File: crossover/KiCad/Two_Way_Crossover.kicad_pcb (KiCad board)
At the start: 2 copper layers, 115.6 x 152.4 mm, 21 parts, among them J1 Conn_01x01_Female, J2 Conn_01x01_Female, J3 Woofer, J4 Tweeter

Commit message: Tweak crossover
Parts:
- moved J2 8.98 mm to (38.7, 105.4)
- moved J3 8.89 mm to (142.9, 78.7)
- moved C1 7.73 mm to (73.0, 95.2)
- moved J1 7.73 mm to (38.7, 95.2)
- moved L1 7.66 mm to (41.3, 67.3)
- moved C4 7.65 mm to (72.4, 38.1)
- moved J4 5.08 mm to (142.9, 95.2)
- moved H1 1.27 mm to (143.5, 29.2)
- moved H2 1.27 mm to (143.5, 171.4)
- moved C3 0.63 mm to (44.5, 117.5)
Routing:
- net Net-(J4-Pad1): track 57.2 -> 108.0 mm
- net Net-(J3-Pad1): track 72.5 -> 79.8 mm
- net Net-(C1-Pad1): track 48.6 -> 55.5 mm
- net Net-(C4-Pad1): track 11.2 -> 5.50 mm
- net Net-(C2-Pad2): track 91.1 -> 86.7 mm
- net Net-(C3-Pad2): track 19.4 -> 20.3 mm
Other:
- board size 115.6 x 152.4 mm -> 116.8 x 152.4 mm
- net class Default: clearance 0.2 -> 0.1524; trace_width 0.25 -> 0.1524; via_dia 0.8 -> 0.508; via_drill 0.4 -> 0.254
- rule pad_to_mask_clearance: 0.051 -> 0.0508
- rule trace_clearance: 0.2 -> 0.1524
- rule trace_min: 0.2 -> 0.1524
- rule via_min_drill: 0.3 -> 0.254
- rule via_min_size: 0.4 -> 0.508

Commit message: Redesign PCB
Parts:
- removed R5, R6: 8R2, Resistor_THT:R_Axial_Power_L60.0mm_W14.0mm_P66.04mm
- L1, L2, L3: footprint Inductor_THT:L_Radial_D40.6mm_P26.16mm_Vishay_IHB-5 -> etal_Inductors:Radial_D36.5mm_H12.0mm_P23.0mm
- R1, R2: footprint Resistor_THT:R_Axial_Power_L60.0mm_W14.0mm_P66.04mm -> etal_Power_Resistor:Resistor_Power_Axial_L91.5_W20.2_H20.2
- R3, R4: value 8R2 -> 4R7
- moved H1 110.5 mm to (33.0, 31.0)
- moved H3 93.2 mm to (130.0, 31.0)
- moved R3 73.4 mm to (113.5, 181.6)
- moved J4 70.1 mm to (126.0, 163.3)
- moved C2 66.5 mm to (114.8, 147.3), turned to 90 degrees
- moved C1 60.3 mm to (47.0, 149.6), turned to 90 degrees
- moved C3 56.6 mm to (100.8, 122.4), turned to 270 degrees
- moved R4 51.6 mm to (113.5, 165.9), turned to 180 degrees
- moved J3 49.9 mm to (126.0, 125.7)
- moved C4 48.9 mm to (49.5, 81.3), turned to 270 degrees
- moved L1 45.1 mm to (76.7, 95.2), turned to 180 degrees
- moved L3 33.0 mm to (114.6, 95.2), turned to 180 degrees
- moved J2 31.1 mm to (34.0, 136.1)
- moved J1 27.3 mm to (34.0, 122.2)
- moved R2 24.8 mm to (81.5, 65.0), turned to 180 degrees
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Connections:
- R4 pad 1: Net-(C3-Pad2) -> Net-(J4-Pad1)
- R4 pad 2: Net-(J4-Pad1) -> GND
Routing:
- net Net-(J4-Pad1): track 108.0 -> 28.2 mm
- net Net-(C3-Pad2): track 20.3 -> 66.5 mm
- net Net-(C2-Pad2): track 86.7 -> 126.9 mm
- net Net-(C4-Pad1): track 5.50 -> 24.8 mm
- net Net-(C1-Pad2): track 35.8 -> 50.0 mm
- net Net-(C1-Pad1): track 55.5 -> 66.4 mm
- net Net-(J3-Pad1): track 79.8 -> 89.7 mm
- removed copper zone on F.Cu, net GND
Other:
- board size 116.8 x 152.4 mm -> 107 x 167 mm

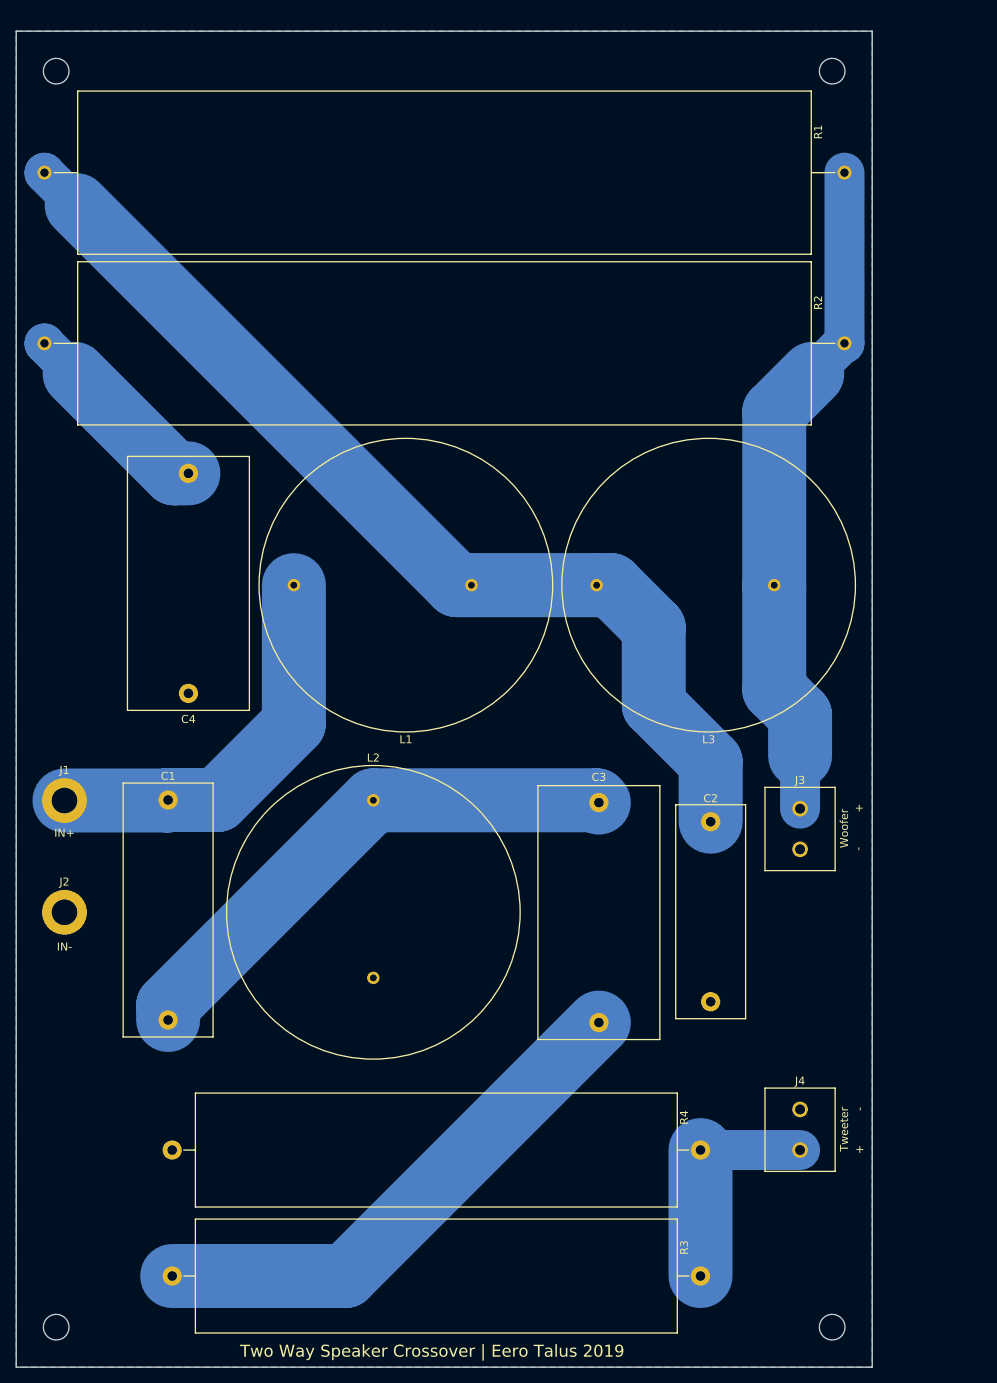
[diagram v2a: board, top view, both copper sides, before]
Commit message: Partially fix incorrect PCB footprints
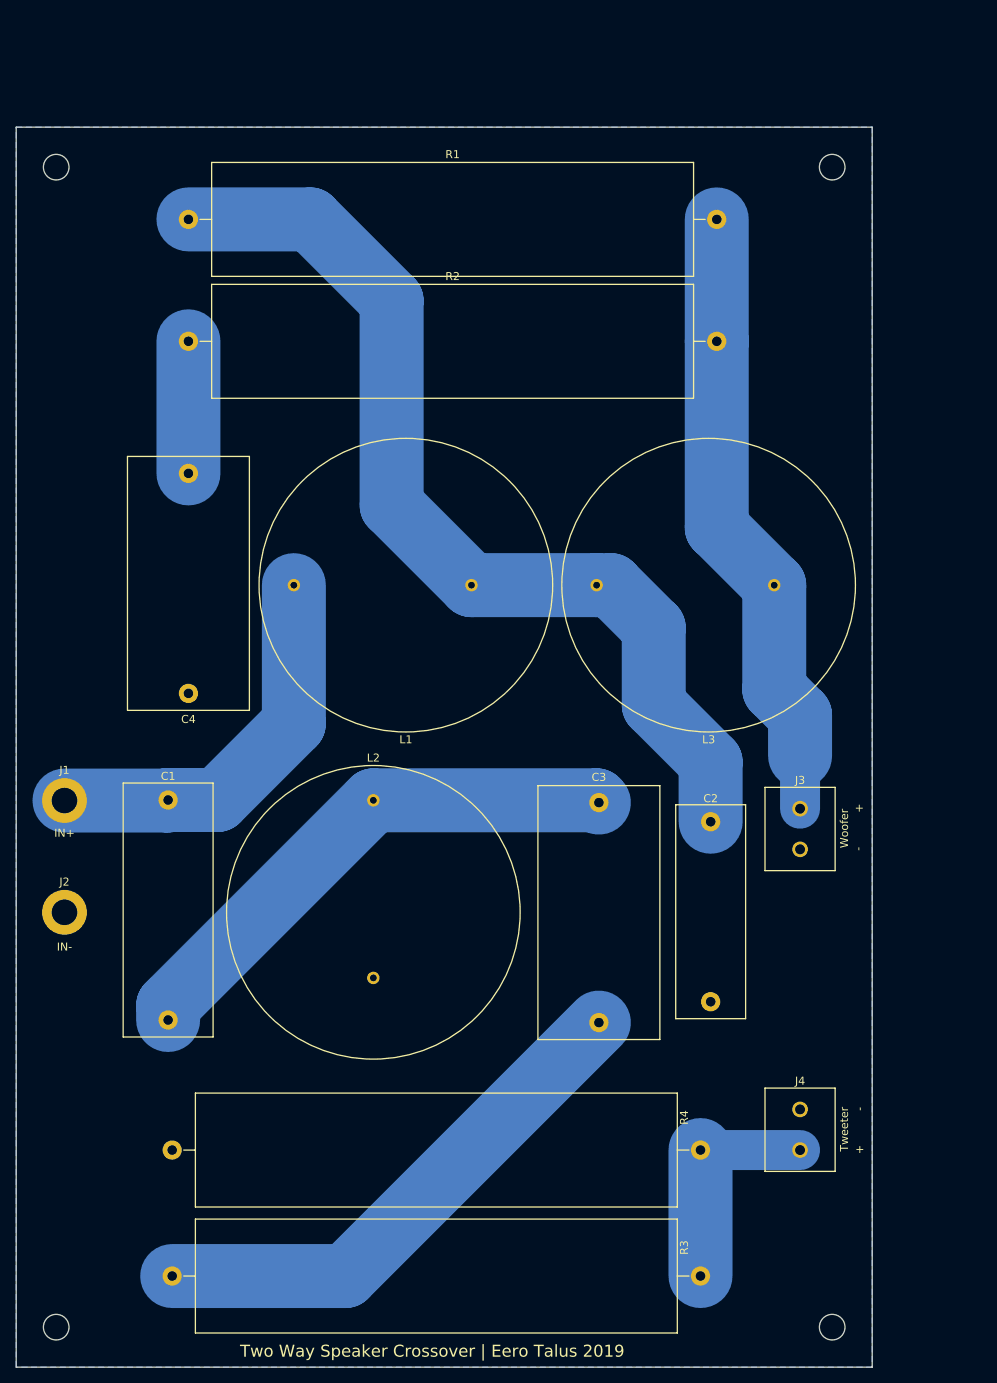
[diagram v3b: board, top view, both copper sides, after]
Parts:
- R1, R2: footprint etal_Power_Resistor:Resistor_Power_Axial_L91.5_W20.2_H20.2 -> Resistor_THT:R_Axial_Power_L60.0mm_W14.0mm_P66.04mm
- moved R1 32.5 mm to (49.5, 49.5), turned to 0 degrees
- moved R2 32.0 mm to (49.5, 64.8), turned to 0 degrees
- moved H1 12.0 mm to (33.0, 43.0)
- moved H3 12.0 mm to (130.0, 43.0)
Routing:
- net Net-(C4-Pad1): track 24.8 -> 16.5 mm
- net Net-(J3-Pad1): track 89.7 -> 83.1 mm
- net Net-(C2-Pad2): track 126.9 -> 121.5 mm
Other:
- board size 107 x 167 mm -> 107 x 155 mm

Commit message: Add license
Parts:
- R3, R4: footprint Resistor_THT:R_Axial_Power_L60.0mm_W14.0mm_P66.04mm -> etal_Resistors_THT:Resistor_Power_Axial_L91.5_W20.2_H20.2
- moved R4 34.5 mm to (81.3, 153.7), turned to 0 degrees
- moved R3 33.0 mm to (81.3, 174.6), turned to 0 degrees
- moved J4 30.0 mm to (127.0, 133.3)
- moved C1 12.1 mm to (49.5, 137.8)
- moved C3 12.0 mm to (101.6, 110.5)
- moved L2 11.9 mm to (74.9, 124.5)
- moved C2 11.4 mm to (114.8, 135.9)
- moved J3 8.32 mm to (127.0, 117.5)
- moved C4 8.25 mm to (49.5, 73.0)
- moved L1 8.25 mm to (76.7, 87.0)
- moved L3 8.25 mm to (114.6, 87.0)
- moved J1 7.62 mm to (34.0, 114.6)
- moved J2 7.62 mm to (34.0, 128.5)
- moved R1 3.81 mm to (49.5, 45.7)
- moved R2 3.81 mm to (49.5, 61.0)
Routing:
- net Net-(J4-Pad1): track 28.2 -> 53.5 mm
- net Net-(C3-Pad2): track 66.5 -> 84.6 mm
- net Net-(C1-Pad2): track 50.0 -> 66.8 mm
- net Net-(J3-Pad1): track 83.1 -> 70.8 mm
- net Net-(C2-Pad2): track 121.5 -> 109.8 mm
- net Net-(C4-Pad1): track 16.5 -> 12.1 mm
- net Net-(C1-Pad1): track 66.4 -> 65.6 mm
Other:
- board text added: "+ Tweeter -"
- board text added: "- Woofer +"
- board text added: "Copyright Eero Talus 2020. This documentation describes Open Hardware and is licensed under the CERN OHL v. 1.2. You may redistribute and modify this documentation under the terms of the CERN OHL v.1.2. (http://ohwr.org/cernohl). This documentation is distributed WITHOUT ANY EXPRESS OR IMPLIED WARRANTY, INCLUDING OF MERCHANTABILITY, SATISFACTORY QUALITY AND FITNESS FOR A PARTICULAR PURPOSE. Pleas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"
- board text added: "Two Way Speaker Crossover Copyright Eero Talus 2019 Licensed under the CERN OHL v1.2 license."
- board text removed: "+"
- board text removed: "-"
- board text removed: "Tweeter"
- board text removed: "Two Way Speaker Crossover | Eero Talus 2019"
- board text removed: "Woofer"
